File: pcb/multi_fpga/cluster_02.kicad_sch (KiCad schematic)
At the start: 7 parts, among them J5 Cluster2_SpokeBus, J6 Cluster2_Power

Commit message: Fixed C footprint.
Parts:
- C8, C9: footprint Capacitor_SMD:C_0201_0603Metric -> Capacitor_SMD:C_0603_1608Metric
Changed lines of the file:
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@@
 			)
 		)
-		(property "Footprint" "Capacitor_SMD:C_0201_0603Metric"
+		(property "Footprint" "Capacitor_SMD:C_0603_1608Metric"
 			(at 322.2752 195.58 0)
 			(hide yes)
@@
 			)
 		)
-		(property "Footprint" "Capacitor_SMD:C_0201_0603Metric"
+		(property "Footprint" "Capacitor_SMD:C_0603_1608Metric"
 			(at 284.1752 195.58 0)
 			(hide yes)

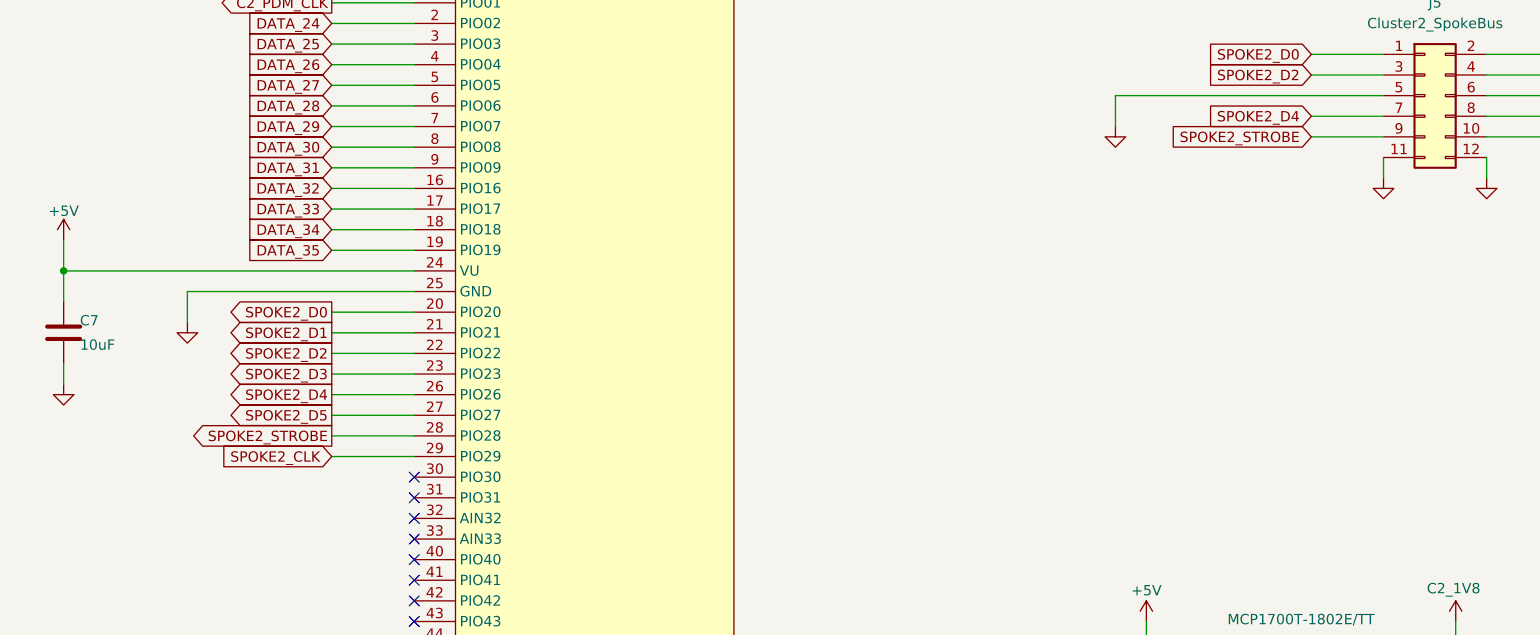
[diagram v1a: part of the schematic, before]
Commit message: Added FPGA_RESET_N signal.
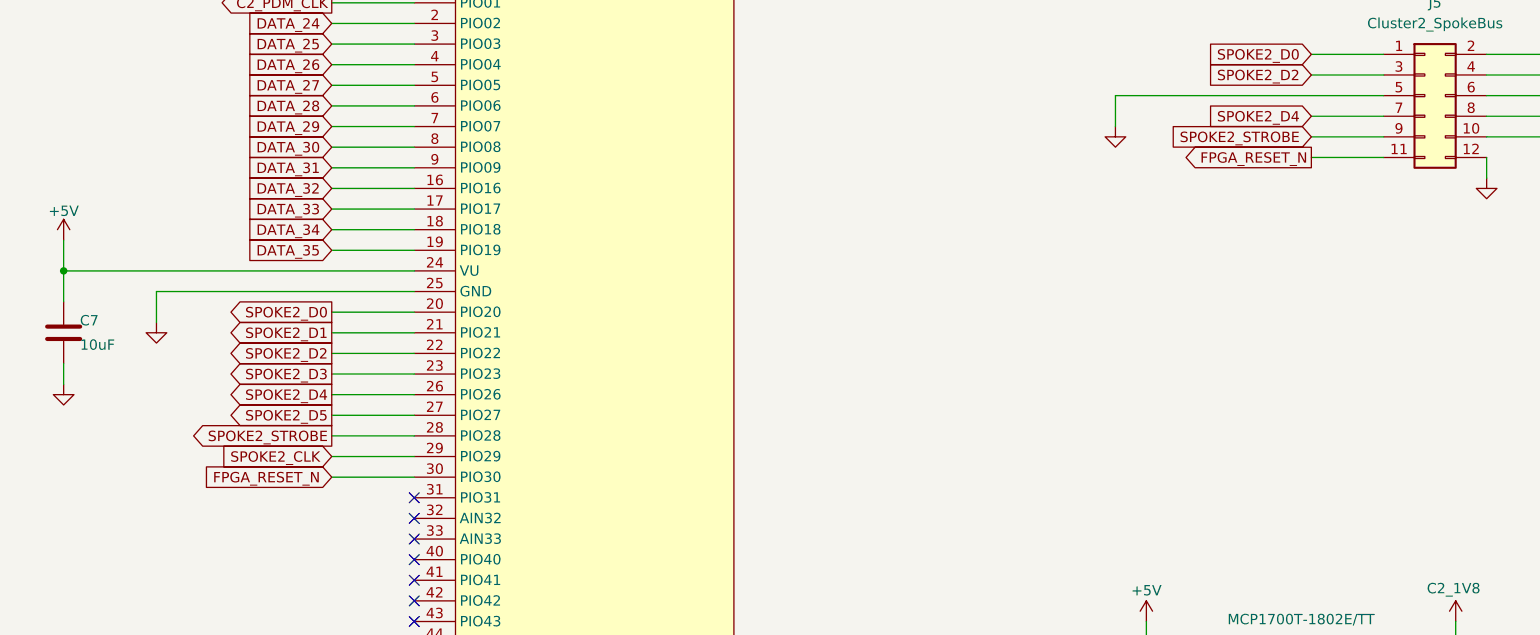
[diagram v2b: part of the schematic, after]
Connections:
- net GND: no longer J5.11 (Pin_11)
- net FPGA_RESET_N: now reaches A3.30 (PIO30)
- net FPGA_RESET_N: now also J5.11 (Pin_11)
- no-connect marks 13 -> 12
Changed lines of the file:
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@@
-	)
-	(no_connect
-		(at 193.04 161.29)
 	)
 	(no_connect
@@
 	(wire
 		(pts
+			(xy 303.53 121.92) (xy 312.42 121.92)
+		)
+		(stroke
+			(width 0)
+			(type default)
+		)
+	)
+	(wire
+		(pts
 			(xy 303.53 109.22) (xy 312.42 109.22)
 		)
@@
 	(wire
 		(pts
+			(xy 193.04 161.29) (xy 182.88 161.29)
+		)
+		(stroke
+			(width 0)
+			(type default)
+		)
+	)
+	(wire
+		(pts
 			(xy 312.42 114.3) (xy 279.4 114.3)
 		)
@@
 	(wire
 		(pts
-			(xy 312.42 121.92) (xy 312.42 124.46)
-		)
-		(stroke
-			(width 0)
-			(type default)
-		)
-	)
-	(wire
-		(pts
 			(xy 193.04 156.21) (xy 182.88 156.21)
 		)
@@
 	(wire
 		(pts
-			(xy 165.1 142.24) (xy 165.1 138.43)
+			(xy 161.29 142.24) (xy 161.29 138.43)
 		)
 		(stroke
@@
 	(wire
 		(pts
-			(xy 165.1 138.43) (xy 193.04 138.43)
+			(xy 161.29 138.43) (xy 193.04 138.43)
 		)
 		(stroke
@@
 			(width 0)
 			(type default)
+		)
+	)
+	(global_label "FPGA_RESET_N"
+		(shape input)
+		(at 182.88 161.29 180)
+		(effects
+			(font
+				(size 1.27 1.27)
+			)
+			(justify right)
+		)
+		(property "Intersheetrefs" "${INTERSHEET_REFS}"
+			(at 182.88 161.29 180)
+			(hide yes)
+			(show_name no)
+			(do_not_autoplace no)
+			(effects
+				(font
+					(size 1.27 1.27)
+				)
+			)
 		)
 	)
@@
 		(property "Intersheetrefs" "${INTERSHEET_REFS}"
 			(at 336.55 119.38 0)
+			(hide yes)
+			(show_name no)
+			(do_not_autoplace no)
+			(effects
+				(font
+					(size 1.27 1.27)
+				)
+			)
+		)
+	)
+	(global_label "FPGA_RESET_N"
+		(shape output)
+		(at 303.53 121.92 180)
+		(effects
+			(font
+				(size 1.27 1.27)
+			)
+			(justify right)
+		)
+		(property "Intersheetrefs" "${INTERSHEET_REFS}"
+			(at 303.53 121.92 180)
 			(hide yes)
 			(show_name no)
@@
 	(symbol
 		(lib_id "power:GND")
-		(at 165.1 142.24 0)
+		(at 161.29 142.24 0)
 		(unit 1)
 		(body_style 1)
@@
 		(dnp no)
 		(property "Reference" "#PWR031"
-			(at 165.1 142.24 0)
+			(at 161.29 142.24 0)
 			(hide yes)
 			(show_name no)
@@
 		)
 		(property "Value" "GND"
-			(at 165.1 142.24 0)
+			(at 161.29 142.24 0)
 			(hide yes)
 			(show_name no)
@@
 		)
 		(property "Footprint" ""
-			(at 165.1 142.24 0)
+			(at 161.29 142.24 0)
 			(hide yes)
 			(show_name no)
@@
 		)
 		(property "Datasheet" ""
-			(at 165.1 142.24 0)
+			(at 161.29 142.24 0)
 			(hide yes)
 			(show_name no)
@@
 		)
 		(property "Description" ""
-			(at 165.1 142.24 0)
+			(at 161.29 142.24 0)
 			(hide yes)
 			(show_name no)
@@
 					(unit 1)
 				)
-			)
-		)
-	)
-	(symbol
-		(lib_name "GND_10")
-		(lib_id "power:GND")
-		(at 312.42 124.46 0)
-		(unit 1)
-		(body_style 1)
-		(exclude_from_sim no)
-		(in_bom yes)
-		(on_board yes)
-		(in_pos_files yes)
-		(dnp no)
-		(property "Reference" "#PWR036"
-			(at 312.42 124.46 0)
-			(hide yes)
-			(show_name no)
-			(do_not_autoplace no)
-			(effects
-				(font
-					(size 1.27 1.27)
-				)
-			)
-		)
-		(property "Value" "GND"
-			(at 312.42 124.46 0)
-			(hide yes)
-			(show_name no)
-			(do_not_autoplace no)
-			(effects
-				(font
-					(size 1.27 1.27)
-				)
-			)
-		)
-		(property "Footprint" ""
-			(at 312.42 124.46 0)
-			(hide yes)
-			(show_name no)
-			(do_not_autoplace no)
-			(effects
-				(font
-					(size 1.27 1.27)
-				)
-			)
-		)
-		(property "Datasheet" ""
-			(at 312.42 124.46 0)
-			(hide yes)
-			(show_name no)
-			(do_not_autoplace no)
-			(effects
-				(font
-					(size 1.27 1.27)
-				)
-			)
-		)
-		(property "Description" "Power symbol creates a global label with name \"GND\" , ground"
-			(at 312.42 124.46 0)
-			(hide yes)
-			(show_name no)
-			(do_not_autoplace no)
-			(effects
-				(font
-					(size 1.27 1.27)
-				)
-			)
-		)
-		(pin "1"
-		)
-		(instances
-			(project "top"
-				(path "/80f109c4-96c5-4385-bfb6-0f7a96b014ab/0b2a1ea7-00c3-4711-b11b-e0de0abfaee6"
-					(reference "#PWR036")
-					(unit 1)
-				)
-			)
-			(project "cluster_02"
-				(path "/bcbf20bc-d0e7-4347-81f7-b5a46e2baf4f"
-					(reference "#PWR036")
-					(unit 1)
-				)

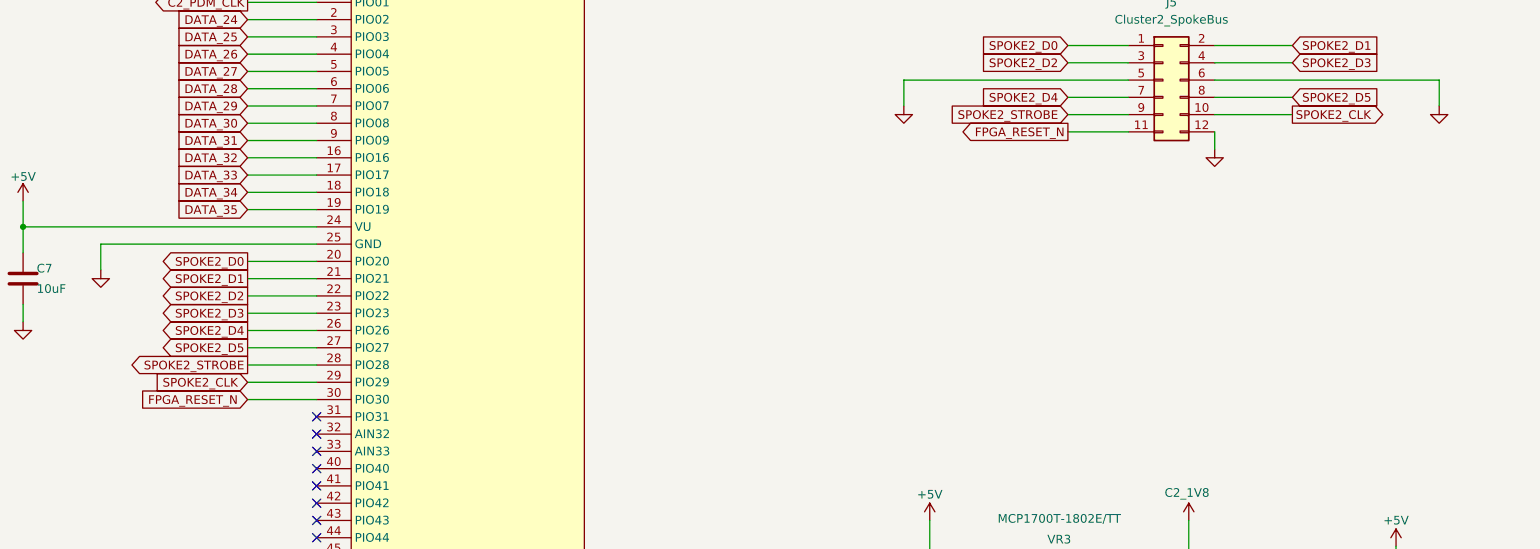
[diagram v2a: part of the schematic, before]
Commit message: Added spoke alive signals.
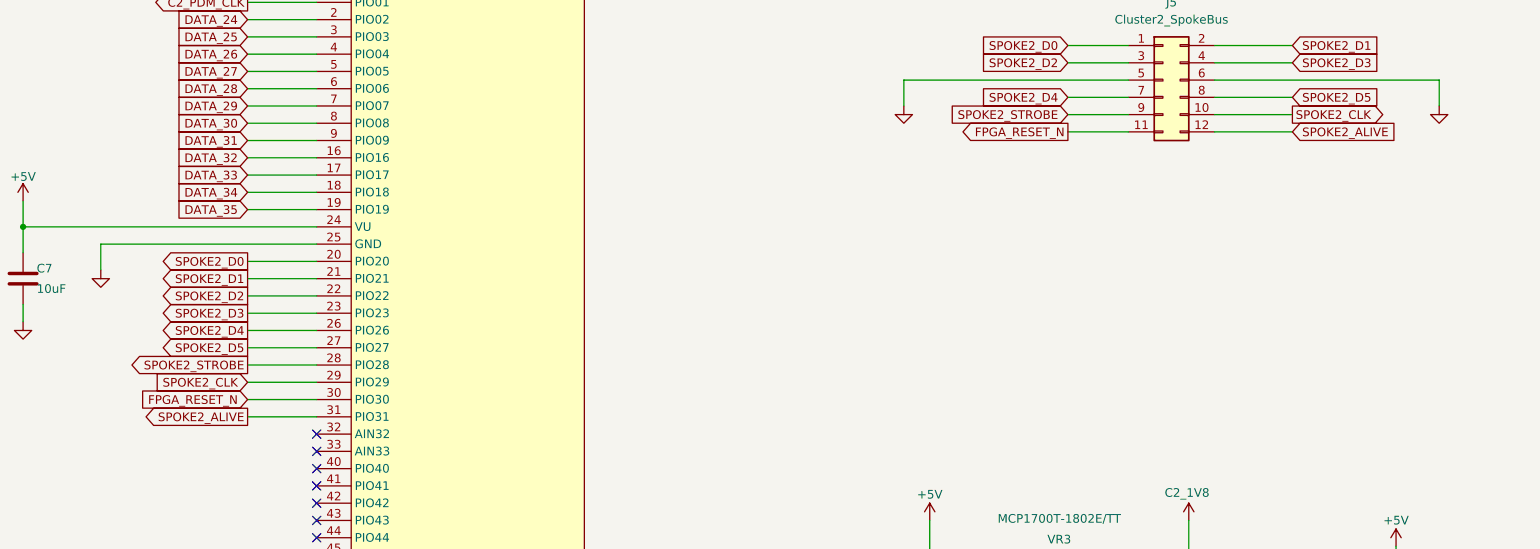
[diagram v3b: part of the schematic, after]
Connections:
- net GND: no longer J5.12 (Pin_12)
- net SPOKE2_ALIVE: now reaches A3.31 (PIO31)
- net SPOKE2_ALIVE: now also J5.12 (Pin_12)
- no-connect marks 12 -> 11
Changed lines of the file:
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@@
-	)
-	(no_connect
-		(at 193.04 163.83)
 	)
 	(no_connect
@@
 	(wire
 		(pts
+			(xy 182.88 163.83) (xy 193.04 163.83)
+		)
+		(stroke
+			(width 0)
+			(type default)
+		)
+	)
+	(wire
+		(pts
 			(xy 303.53 109.22) (xy 312.42 109.22)
 		)
@@
 	(wire
 		(pts
-			(xy 325.12 121.92) (xy 325.12 124.46)
-		)
-		(stroke
-			(width 0)
-			(type default)
-		)
-	)
-	(wire
-		(pts
 			(xy 358.14 114.3) (xy 358.14 118.11)
 		)
@@
 		(pts
 			(xy 193.04 146.05) (xy 182.88 146.05)
+		)
+		(stroke
+			(width 0)
+			(type default)
+		)
+	)
+	(wire
+		(pts
+			(xy 325.12 121.92) (xy 336.55 121.92)
 		)
 		(stroke
@@
 		)
 	)
+	(global_label "SPOKE2_ALIVE"
+		(shape output)
+		(at 182.88 163.83 180)
+		(fields_autoplaced yes)
+		(effects
+			(font
+				(size 1.27 1.27)
+			)
+			(justify right)
+		)
+		(property "Intersheetrefs" "${INTERSHEET_REFS}"
+			(at 166.5296 163.83 0)
+			(hide yes)
+			(show_name no)
+			(do_not_autoplace no)
+			(effects
+				(font
+					(size 1.27 1.27)
+				)
+				(justify right)
+			)
+		)
+	)
 	(global_label "SPOKE2_D3"
 		(shape output)
@@
 					(size 1.27 1.27)
 				)
+			)
+		)
+	)
+	(global_label "SPOKE2_ALIVE"
+		(shape input)
+		(at 336.55 121.92 0)
+		(fields_autoplaced yes)
+		(effects
+			(font
+				(size 1.27 1.27)
+			)
+			(justify left)
+		)
+		(property "Intersheetrefs" "${INTERSHEET_REFS}"
+			(at 352.9004 121.92 0)
+			(hide yes)
+			(show_name no)
+			(do_not_autoplace no)
+			(effects
+				(font
+					(size 1.27 1.27)
+				)
+				(justify left)
 			)
 		)
@@
 					(unit 1)
 				)
-			)
-		)
-	)
-	(symbol
-		(lib_name "GND_11")
-		(lib_id "power:GND")
-		(at 325.12 124.46 0)
-		(unit 1)
-		(body_style 1)
-		(exclude_from_sim no)
-		(in_bom yes)
-		(on_board yes)
-		(in_pos_files yes)
-		(dnp no)
-		(property "Reference" "#PWR039"
-			(at 325.12 124.46 0)
-			(hide yes)
-			(show_name no)
-			(do_not_autoplace no)
-			(effects
-				(font
-					(size 1.27 1.27)
-				)
-			)
-		)
-		(property "Value" "GND"
-			(at 325.12 124.46 0)
-			(hide yes)
-			(show_name no)
-			(do_not_autoplace no)
-			(effects
-				(font
-					(size 1.27 1.27)
-				)
-			)
-		)
-		(property "Footprint" ""
-			(at 325.12 124.46 0)
-			(hide yes)
-			(show_name no)
-			(do_not_autoplace no)
-			(effects
-				(font
-					(size 1.27 1.27)
-				)
-			)
-		)
-		(property "Datasheet" ""
-			(at 325.12 124.46 0)
-			(hide yes)
-			(show_name no)
-			(do_not_autoplace no)
-			(effects
-				(font
-					(size 1.27 1.27)
-				)
-			)
-		)
-		(property "Description" "Power symbol creates a global label with name \"GND\" , ground"
-			(at 325.12 124.46 0)
-			(hide yes)
-			(show_name no)
-			(do_not_autoplace no)
-			(effects
-				(font
-					(size 1.27 1.27)
-				)
-			)
-		)
-		(pin "1"
-		)
-		(instances
-			(project "top"
-				(path "/80f109c4-96c5-4385-bfb6-0f7a96b014ab/0b2a1ea7-00c3-4711-b11b-e0de0abfaee6"
-					(reference "#PWR039")
-					(unit 1)
-				)
-			)
-			(project "cluster_02"
-				(path "/bcbf20bc-d0e7-4347-81f7-b5a46e2baf4f"
-					(reference "#PWR039")
-					(unit 1)
-				)

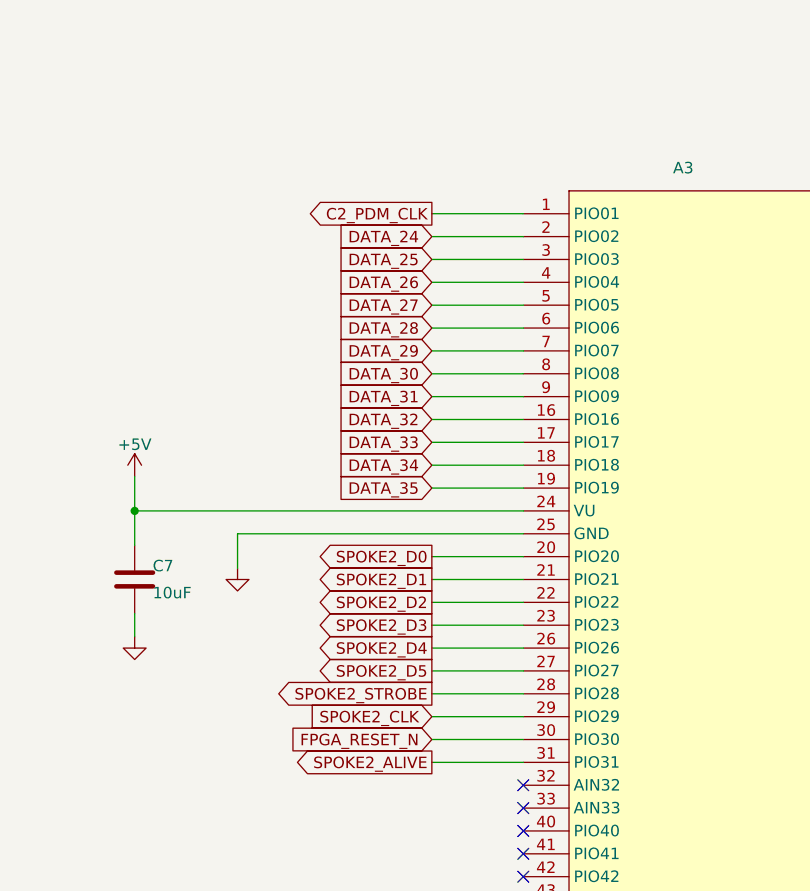
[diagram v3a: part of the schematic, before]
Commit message: Switched to use only cluster_00 pcb.
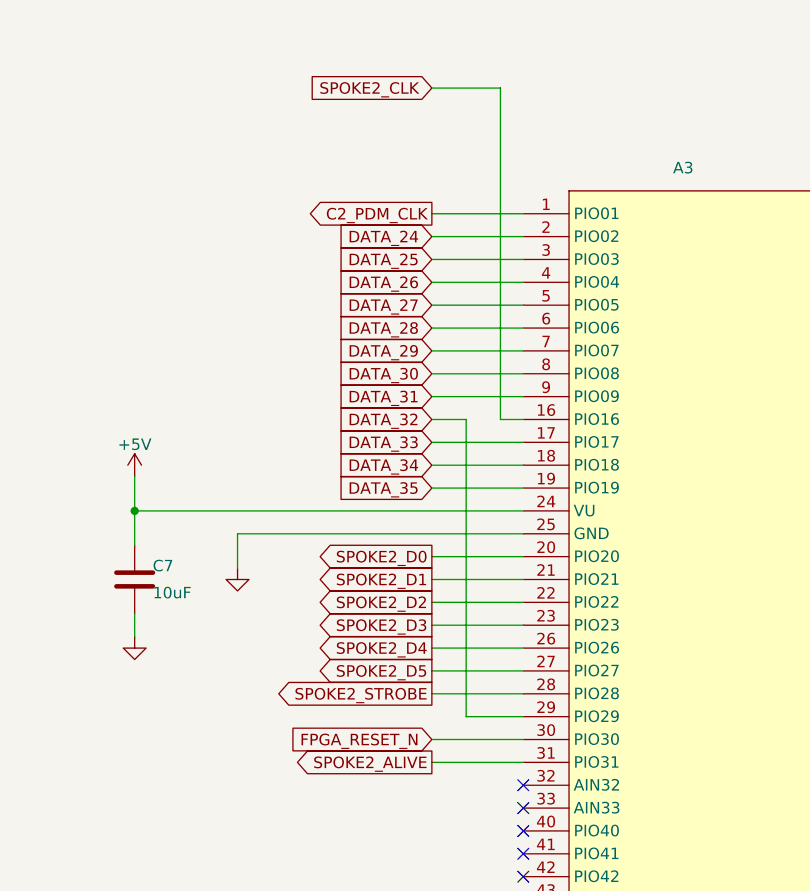
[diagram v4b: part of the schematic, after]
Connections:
- net DATA_32: now also A3.29 (PIO29); no longer A3.16 (PIO16)
- net SPOKE2_CLK: now also A3.16 (PIO16); no longer A3.29 (PIO29)
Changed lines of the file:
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@@
 	(wire
 		(pts
-			(xy 193.04 158.75) (xy 182.88 158.75)
+			(xy 193.04 158.75) (xy 186.69 158.75)
 		)
 		(stroke
@@
 	(wire
 		(pts
+			(xy 193.04 125.73) (xy 190.5 125.73)
+		)
+		(stroke
+			(width 0)
+			(type default)
+		)
+	)
+	(wire
+		(pts
 			(xy 149.86 132.08) (xy 149.86 139.7)
 		)
@@
 	(wire
 		(pts
+			(xy 190.5 88.9) (xy 182.88 88.9)
+		)
+		(stroke
+			(width 0)
+			(type default)
+		)
+	)
+	(wire
+		(pts
 			(xy 193.04 120.65) (xy 182.88 120.65)
 		)
@@
 	(wire
 		(pts
+			(xy 186.69 125.73) (xy 186.69 158.75)
+		)
+		(stroke
+			(width 0)
+			(type default)
+		)
+	)
+	(wire
+		(pts
 			(xy 193.04 148.59) (xy 182.88 148.59)
 		)
@@
 	(wire
 		(pts
-			(xy 193.04 125.73) (xy 182.88 125.73)
-		)
-		(stroke
-			(width 0)
-			(type default)
-		)
-	)
-	(wire
-		(pts
 			(xy 193.04 118.11) (xy 182.88 118.11)
 		)
@@
 	(wire
 		(pts
+			(xy 182.88 125.73) (xy 186.69 125.73)
+		)
+		(stroke
+			(width 0)
+			(type default)
+		)
+	)
+	(wire
+		(pts
 			(xy 303.53 119.38) (xy 312.42 119.38)
+		)
+		(stroke
+			(width 0)
+			(type default)
+		)
+	)
+	(wire
+		(pts
+			(xy 190.5 125.73) (xy 190.5 88.9)
 		)
 		(stroke
@@
 	(global_label "SPOKE2_CLK"
 		(shape input)
-		(at 182.88 158.75 180)
-		(effects
-			(font
-				(size 1.27 1.27)
-			)
-			(justify right)
-		)
-		(property "Intersheetrefs" "${INTERSHEET_REFS}"
-			(at 182.88 158.75 180)
-			(hide yes)
-			(show_name no)
+		(at 182.88 88.9 180)
+		(effects
+			(font
+				(size 1.27 1.27)
+			)
+			(justify right)
+		)
+		(property "Intersheetrefs" "${INTERSHEET_REFS}"
+			(at 182.88 88.9 180)
+			(hide yes)
+			(show_name no)
